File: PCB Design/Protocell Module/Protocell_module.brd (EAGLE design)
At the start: 70.8 x 27.9 mm, 19 parts, among them IC1 MC7805BDTRKG, X3 RJ45-8X

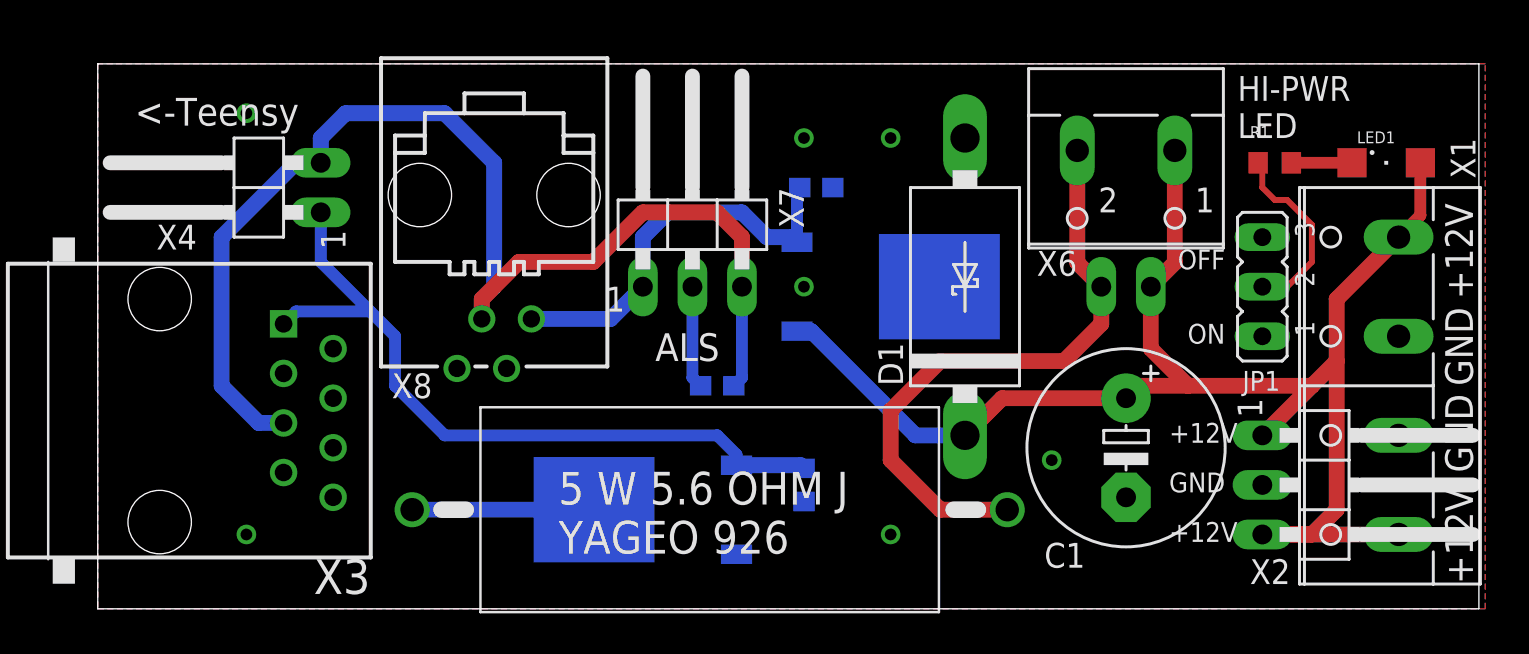
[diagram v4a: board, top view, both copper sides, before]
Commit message: Added labels to silkscreen
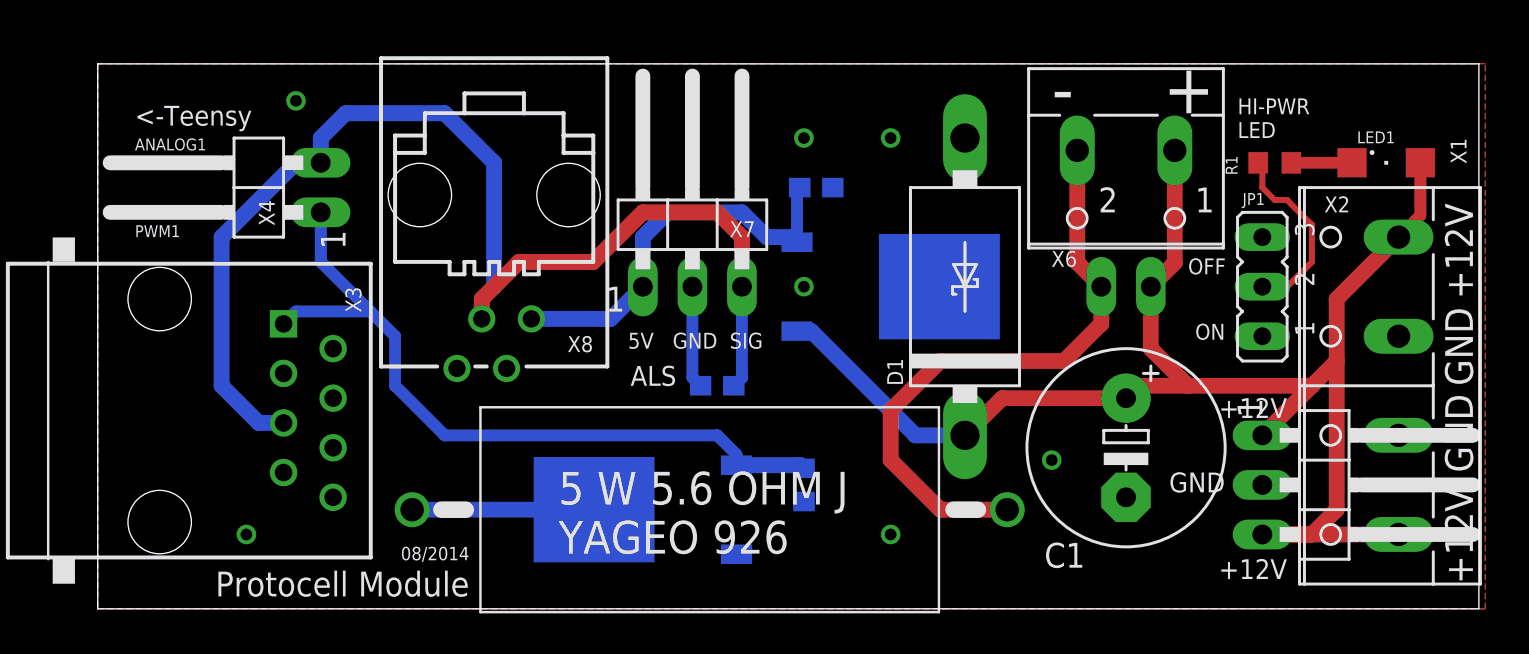
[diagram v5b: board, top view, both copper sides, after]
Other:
- board text added: "+"
- board text added: "-"
- board text added: "08/2014"
- board text added: "5V"
- board text added: "ANALOG1"
- board text added: "PWM1"
- board text added: "Protocell Module"
- board text added: "SIG"
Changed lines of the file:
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@@
 <wire x1="70.79" y1="27.93" x2="0" y2="27.93" width="0" layer="20"/>
 <wire x1="0" y1="27.93" x2="0" y2="0" width="0" layer="20"/>
-<text x="1.905" y="24.765" size="1.4224" layer="21" ratio="17">&lt;-Teensy</text>
+<text x="1.905" y="24.765" size="1.016" layer="21" ratio="17">&lt;-Teensy</text>
 <text x="70.485" y="15.875" size="1.4224" layer="21" ratio="17" rot="R90">+12V</text>
 <text x="70.485" y="1.27" size="1.4224" layer="21" ratio="17" rot="R90">+12V</text>
@@
 <text x="70.485" y="5.715" size="1.4224" layer="22" ratio="17" rot="MR270">+12V</text>
 <text x="70.485" y="20.955" size="1.4224" layer="22" ratio="17" rot="MR270">+12V</text>
-<text x="58.42" y="24.13" size="1.27" layer="21" ratio="17">HI-PWR
+<text x="58.42" y="24.13" size="0.8128" layer="21" ratio="17">HI-PWR
 LED</text>
-<text x="28.575" y="12.7" size="1.4224" layer="21" ratio="17">ALS</text>
+<text x="27.305" y="11.43" size="1.016" layer="21" ratio="17">ALS</text>
 <text x="57.785" y="5.715" size="1.016" layer="22" ratio="17" rot="MR0">GND</text>
 <text x="57.785" y="6.985" size="1.016" layer="21" ratio="17" rot="R180">GND</text>
-<text x="58.42" y="4.445" size="1.016" layer="21" ratio="17" rot="R180">+12V</text>
-<text x="58.42" y="9.525" size="1.016" layer="21" ratio="17" rot="R180">+12V</text>
+<text x="60.96" y="2.54" size="1.016" layer="21" ratio="17" rot="R180">+12V</text>
+<text x="60.96" y="10.795" size="1.016" layer="21" ratio="17" rot="R180">+12V</text>
 <text x="57.785" y="8.255" size="1.016" layer="22" ratio="17" rot="MR0">+12V</text>
 <text x="57.785" y="3.175" size="1.016" layer="22" ratio="17" rot="MR0">+12V</text>
-<text x="57.785" y="14.605" size="1.016" layer="21" ratio="17" rot="R180">ON</text>
-<text x="57.785" y="18.415" size="1.016" layer="21" ratio="17" rot="R180">OFF</text>
+<text x="57.785" y="14.605" size="0.8128" layer="21" ratio="17" rot="R180">ON</text>
+<text x="55.88" y="17.145" size="0.8128" layer="21" ratio="17">OFF</text>
+<text x="19.05" y="1.905" size="1.27" layer="21" font="vector" ratio="15" rot="R180">Protocell Module</text>
+<text x="19.05" y="3.175" size="0.6858" layer="21" font="vector" ratio="10" rot="R180">08/2014</text>
+<text x="31.75" y="22.86" size="0.8128" layer="22" font="vector" ratio="10" rot="MR0">08/2014</text>
+<text x="31.75" y="24.765" size="1.27" layer="22" font="vector" ratio="15" rot="MR0">Protocell Module</text>
+<text x="54.61" y="25.4" size="2.54" layer="21" font="vector" ratio="20">+</text>
+<text x="56.515" y="25.4" size="2.54" layer="22" font="vector" ratio="20" rot="MR0">+</text>
+<text x="50.8" y="25.4" size="2.54" layer="22" font="vector" ratio="20" rot="MR0">-</text>
+<text x="48.895" y="25.4" size="2.54" layer="21" font="vector" ratio="20">-</text>
+<text x="32.385" y="13.335" size="0.8128" layer="21" font="vector" ratio="6">SIG</text>
+<text x="29.464" y="13.335" size="0.8128" layer="21" font="vector" ratio="6">GND</text>
+<text x="27.178" y="13.335" size="0.8128" layer="21" font="vector" ratio="6">5V</text>
+<text x="28.702" y="13.335" size="0.8128" layer="22" font="vector" ratio="6" rot="MR0">5V</text>
+<text x="31.496" y="13.335" size="0.8128" layer="22" font="vector" ratio="6" rot="MR0">GND</text>
+<text x="34.29" y="13.335" size="0.8128" layer="22" font="vector" ratio="6" rot="MR0">SIG</text>
+<text x="1.905" y="19.05" size="0.6096" layer="21" font="vector" ratio="6">PWM1</text>
+<text x="1.905" y="23.495" size="0.6096" layer="21" font="vector" ratio="6">ANALOG1</text>
+<text x="5.715" y="23.495" size="0.6096" layer="22" font="vector" ratio="6" rot="MR0">ANALOG1</text>
+<text x="4.445" y="19.05" size="0.6096" layer="22" font="vector" ratio="6" rot="MR0">PWM1</text>
 </plain>
 <attributes>
@@
 </element>
 <element name="C2" library="rcl" package="C0603" value="1uF" x="36.83" y="21.59" smashed="yes" rot="MR180">
-<attribute name="NAME" x="36.195" y="23.495" size="1.27" layer="26" rot="MR180"/>
-<attribute name="VALUE" x="34.925" y="20.955" size="1.27" layer="28" rot="MR180"/>
+<attribute name="NAME" x="36.195" y="23.495" size="0.8128" layer="26" rot="MR180"/>
+<attribute name="VALUE" x="35.56" y="20.32" size="0.8128" layer="28" rot="MR180"/>
 </element>
 <element name="X8" library="CBLA_Test_bed_Library" package="558872-1" value="" x="20.32" y="20.32" smashed="yes" rot="R180">
@@
 <attribute name="MF" value="TYCO ELECTRONICS" x="20.32" y="20.32" size="1.778" layer="27" rot="R180" display="off"/>
 <attribute name="OC_FARNELL" value="1557674" x="20.32" y="20.32" size="1.778" layer="27" rot="R180" display="off"/>
-<attribute name="NAME" x="17.145" y="12.065" size="1.27" layer="25" rot="R180"/>
+<attribute name="NAME" x="25.4" y="13.97" size="0.8128" layer="25" rot="R180"/>
 <attribute name="VALUE" x="11.176" y="25.4" size="1.778" layer="27" rot="R270"/>
 </element>
@@
 <attribute name="MF" value="" x="3.175" y="10.16" size="1.778" layer="27" rot="R270" display="off"/>
 <attribute name="OC_FARNELL" value="unknown" x="3.175" y="10.16" size="1.778" layer="27" rot="R270" display="off"/>
-<attribute name="NAME" x="13.97" y="2.54" size="1.778" layer="25" rot="R180"/>
+<attribute name="NAME" x="12.7" y="16.51" size="0.8128" layer="25" rot="R270"/>
 <attribute name="VALUE" x="5.715" y="15.875" size="1.778" layer="27" rot="R270"/>
 </element>
 <element name="T1" library="CBLA_Test_bed_Library" package="DPACK" value="" x="27.94" y="5.08" smashed="yes" rot="MR270">
-<attribute name="NAME" x="22.225" y="1.27" size="1.27" layer="26" rot="MR0"/>
+<attribute name="NAME" x="22.225" y="1.27" size="0.8128" layer="26" rot="MR0"/>
 <attribute name="VALUE" x="30.48" y="0" size="1.27" layer="28" rot="MR0"/>
 </element>
@@
 <attribute name="OC_FARNELL" value="unknown" x="52.705" y="22.225" size="1.778" layer="27" rot="R180" display="off"/>
 <attribute name="VALUE" x="57.745" y="29.845" size="1.27" layer="27" ratio="10" rot="R180"/>
-<attribute name="NAME" x="50.2012" y="18.3388" size="1.27" layer="25" ratio="10" rot="R180"/>
+<attribute name="NAME" x="50.2012" y="18.3388" size="0.8128" layer="25" ratio="10" rot="R180"/>
 </element>
 <element name="IC1" library="CBLA_Test_bed_Library" package="DPACK_3" value="MC7805BDTRKG" x="40.64" y="16.51" smashed="yes" rot="MR90">
@@
 </element>
 <element name="X7" library="CBLA_Test_bed_Library" package="1X03/90" value="" x="30.48" y="20.32" smashed="yes">
-<attribute name="NAME" x="34.925" y="21.59" size="1.27" layer="25" ratio="10" rot="R270"/>
+<attribute name="NAME" x="32.385" y="19.05" size="0.8128" layer="25" ratio="10"/>
 <attribute name="VALUE" x="36.195" y="16.51" size="1.27" layer="27" rot="R90"/>
 </element>
 <element name="X4" library="CBLA_Test_bed_Library" package="1X02/90" value="" x="7.62" y="21.59" smashed="yes" rot="R90">
-<attribute name="NAME" x="5.08" y="19.685" size="1.27" layer="25" ratio="10" rot="R180"/>
+<attribute name="NAME" x="8.255" y="20.955" size="0.8128" layer="25" ratio="10" rot="R270"/>
 <attribute name="VALUE" x="11.43" y="26.035" size="1.27" layer="27" rot="R180"/>
 </element>
 <element name="X5" library="CBLA_Test_bed_Library" package="1X02/90" value="" x="52.705" y="20.32" smashed="yes" rot="MR0">
-<attribute name="NAME" x="57.785" y="19.05" size="1.27" layer="26" ratio="10" rot="MR0"/>
+<attribute name="NAME" x="57.785" y="19.05" size="0.8128" layer="26" ratio="10" rot="MR0"/>
 <attribute name="VALUE" x="48.26" y="16.51" size="1.27" layer="28" rot="MR90"/>
 </element>
 <element name="X2" library="CBLA_Test_bed_Library" package="1X03/90" value="" x="63.5" y="6.35" smashed="yes" rot="R270">
-<attribute name="NAME" x="59.055" y="1.27" size="1.27" layer="25" ratio="10"/>
+<attribute name="NAME" x="62.865" y="20.32" size="0.8128" layer="25" ratio="10"/>
 <attribute name="VALUE" x="59.69" y="0.635" size="1.27" layer="27"/>
 </element>
 <element name="D1" library="CBLA_Test_bed_Library" package="DO201T15" value="SB540E-G" x="44.45" y="16.51" smashed="yes" rot="R90">
-<attribute name="NAME" x="41.275" y="11.43" size="1.27" layer="25" ratio="10" rot="R90"/>
+<attribute name="NAME" x="41.275" y="11.43" size="0.8128" layer="25" ratio="10" rot="R90"/>
 <attribute name="VALUE" x="46.609" y="13.97" size="0.6096" layer="27" ratio="10" rot="R90"/>
 </element>
@@
 </element>
 <element name="R1" library="CBLA_Test_bed_Library" package="R0603" value="470" x="60.325" y="22.86" smashed="yes">
-<attribute name="NAME" x="59.055" y="24.13" size="0.6096" layer="25"/>
-<attribute name="VALUE" x="59.055" y="20.955" size="0.6096" layer="27"/>
+<attribute name="NAME" x="58.42" y="22.225" size="0.6096" layer="25" rot="R90"/>
+<attribute name="VALUE" x="62.865" y="22.225" size="0.6096" layer="27" rot="R90"/>
 </element>
 <element name="X1" library="con-wago-508" package="W237-4P" value="" x="66.04" y="11.43" smashed="yes" rot="R90">
@@
 <attribute name="OC_FARNELL" value="unknown" x="93.98" y="11.43" size="1.778" layer="27" rot="R90" display="off"/>
 <attribute name="VALUE" x="70.358" y="2.54" size="1.27" layer="27" ratio="10" rot="R90"/>
-<attribute name="NAME" x="69.342" y="24.13" size="1.27" layer="25" ratio="10" rot="R270"/>
+<attribute name="NAME" x="69.342" y="24.13" size="0.8128" layer="25" ratio="10" rot="R270"/>
 </element>
 <element name="JP1" library="jumper" package="JP2" value="" x="59.69" y="16.51" smashed="yes" rot="R90">
-<attribute name="NAME" x="58.674" y="11.176" size="1.016" layer="25" ratio="10"/>
+<attribute name="NAME" x="58.674" y="20.701" size="0.6096" layer="25" ratio="10"/>
 <attribute name="VALUE" x="64.008" y="12.954" size="1.27" layer="27" ratio="10" rot="R90"/>
 </element>
@@
 <via x="48.895" y="7.62" extent="1-16" drill="0.6"/>
 <via x="36.195" y="16.51" extent="1-16" drill="0.6"/>
-<via x="7.62" y="25.4" extent="1-16" drill="0.6"/>
+<via x="10.16" y="26.035" extent="1-16" drill="0.6"/>
 <via x="7.62" y="3.81" extent="1-16" drill="0.6"/>
 </signal>

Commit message: Generated gerber files
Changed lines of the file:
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@@
 </class>
 </classes>
-<designrules name="default *">
-<description language="de">&lt;b&gt;EAGLE Design Rules&lt;/b&gt;
-&lt;p&gt;
-Die Standard-Design-Rules sind so gewählt, dass sie für
-die meisten Anwendungen passen. Sollte ihre Platine
-besondere Anforderungen haben, treffen Sie die erforderlichen
-Einstellungen hier und speichern die Design Rules unter
-einem neuen Namen ab.</description>
+<designrules name="SparkFun">
 <description language="en">&lt;b&gt;EAGLE Design Rules&lt;/b&gt;
 &lt;p&gt;
@@
 <param name="mtCopper" value="0.035mm 0.035mm 0.035mm 0.035mm 0.035mm 0.035mm 0.035mm 0.035mm 0.035mm 0.035mm 0.035mm 0.035mm 0.035mm 0.035mm 0.035mm 0.035mm"/>
 <param name="mtIsolate" value="1.5mm 0.15mm 0.2mm 0.15mm 0.2mm 0.15mm 0.2mm 0.15mm 0.2mm 0.15mm 0.2mm 0.15mm 0.2mm 0.15mm 0.2mm"/>
-<param name="mdWireWire" value="10mil"/>
-<param name="mdWirePad" value="10mil"/>
-<param name="mdWireVia" value="10mil"/>
-<param name="mdPadPad" value="10mil"/>
-<param name="mdPadVia" value="10mil"/>
-<param name="mdViaVia" value="10mil"/>
+<param name="mdWireWire" value="8mil"/>
+<param name="mdWirePad" value="8mil"/>
+<param name="mdWireVia" value="8mil"/>
+<param name="mdPadPad" value="8mil"/>
+<param name="mdPadVia" value="8mil"/>
+<param name="mdViaVia" value="8mil"/>
 <param name="mdSmdPad" value="8mil"/>
 <param name="mdSmdVia" value="8mil"/>
@@
 <param name="mdViaViaSameLayer" value="8mil"/>
 <param name="mnLayersViaInSmd" value="2"/>
-<param name="mdCopperDimension" value="40mil"/>
+<param name="mdCopperDimension" value="10mil"/>
 <param name="mdDrill" value="8mil"/>
 <param name="mdSmdStop" value="0mil"/>
-<param name="msWidth" value="10mil"/>
+<param name="msWidth" value="8mil"/>
 <param name="msDrill" value="20mil"/>
 <param name="msMicroVia" value="9.99mm"/>
@@
 <param name="rvMicroViaOuter" value="0.25"/>
 <param name="rvMicroViaInner" value="0.25"/>
-<param name="rlMinPadTop" value="10mil"/>
+<param name="rlMinPadTop" value="12mil"/>
 <param name="rlMaxPadTop" value="20mil"/>
 <param name="rlMinPadInner" value="10mil"/>
 <param name="rlMaxPadInner" value="20mil"/>
-<param name="rlMinPadBottom" value="10mil"/>
+<param name="rlMinPadBottom" value="12mil"/>
 <param name="rlMaxPadBottom" value="20mil"/>
-<param name="rlMinViaOuter" value="8mil"/>
+<param name="rlMinViaOuter" value="10mil"/>
 <param name="rlMaxViaOuter" value="20mil"/>
-<param name="rlMinViaInner" value="8mil"/>
+<param name="rlMinViaInner" value="10mil"/>
 <param name="rlMaxViaInner" value="20mil"/>
 <param name="rlMinMicroViaOuter" value="4mil"/>
@@
 <param name="mlMinCreamFrame" value="0mil"/>
 <param name="mlMaxCreamFrame" value="0mil"/>
-<param name="mlViaStopLimit" value="0mil"/>
+<param name="mlViaStopLimit" value="25mil"/>
 <param name="srRoundness" value="0"/>
 <param name="srMinRoundness" value="0mil"/>
